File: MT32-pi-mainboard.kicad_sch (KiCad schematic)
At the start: 20 parts, among them J1 RPi, J2 MIDI In, J3 LCD2004, J4 5V, J5 LCD2004, SW1 Encoder, SW2 Button 1, SW3 Button 2, SW4 Power, U1 6N138

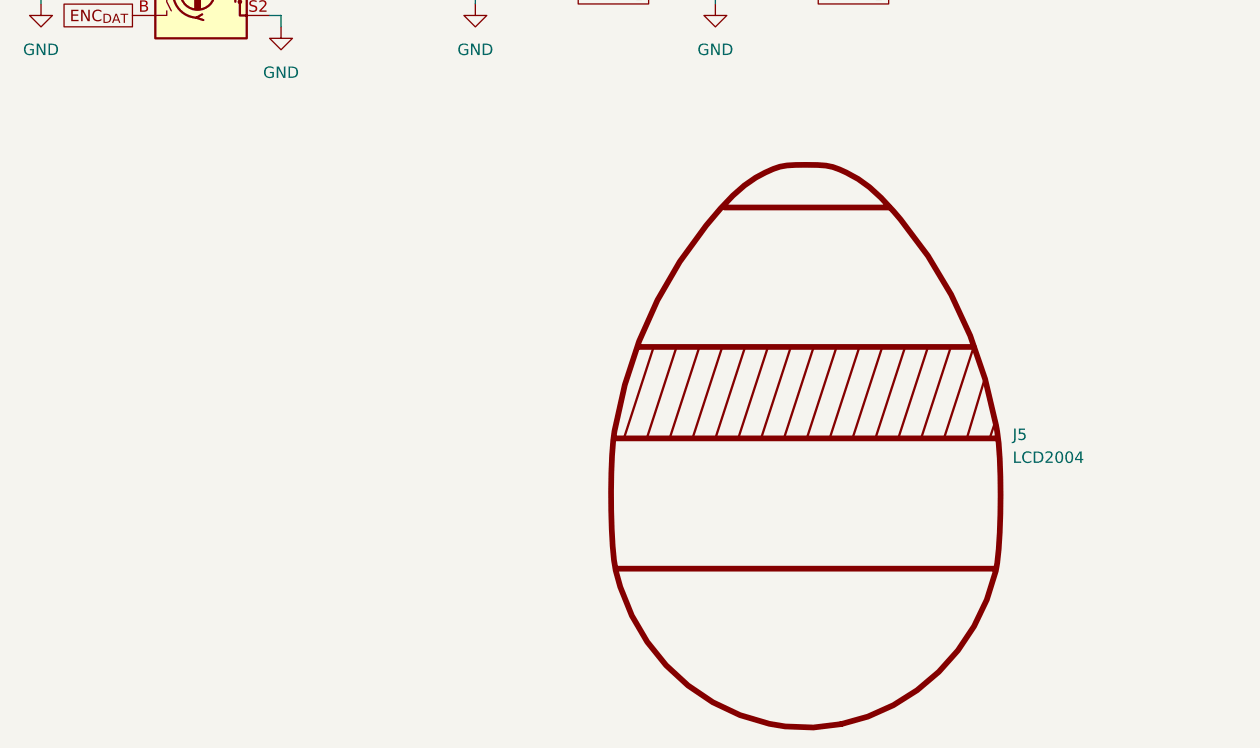
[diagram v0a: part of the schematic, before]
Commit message: add symbols for virtual models and graphics
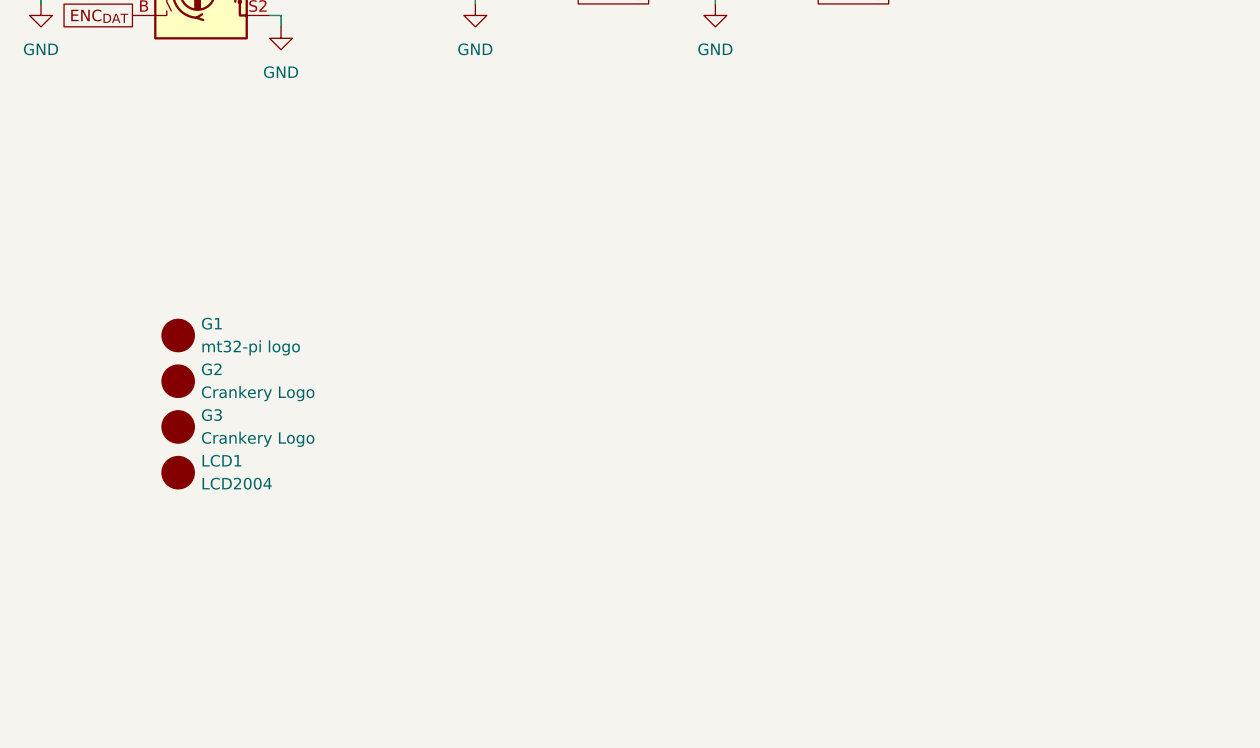
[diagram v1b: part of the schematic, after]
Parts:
- removed J5: LCD2004, 0:LCD2004, symbol Graphic:SYM_EasterEgg_42x60mm
- added G1: mt32-pi logo, 0:mt32-pi-logo, symbol 0:MT32-pi_Logo
- added G2, G3: Crankery Logo, 0:crankery_small, symbol 0:CrankeryLogo
- added LCD1: LCD2004, 0:LCD2004, symbol 0:LCD2004
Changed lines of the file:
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@@
-	)
-	(symbol
-		(lib_id "Graphic:SYM_EasterEgg_42x60mm")
-		(at 119.38 190.5 0)
-		(unit 1)
-		(exclude_from_sim no)
-		(in_bom no)
-		(on_board yes)
-		(dnp no)
-		(fields_autoplaced yes)
-		(property "Reference" "J5"
-			(at 142.24 158.3465 0)
-			(effects
-				(font
-					(size 1.27 1.27)
-				)
-				(justify left)
-			)
-		)
-		(property "Value" "LCD2004"
-			(at 142.24 160.8865 0)
-			(effects
-				(font
-					(size 1.27 1.27)
-				)
-				(justify left)
-			)
-		)
-		(property "Footprint" "0:LCD2004"
-			(at 119.38 194.31 0)
-			(effects
-				(font
-					(size 1.27 1.27)
-				)
-				(hide yes)
-			)
-		)
-		(property "Datasheet" "https://eur-lex.europa.eu/LexUriServ/LexUriServ.do?uri=OJ:L:2013:347:0671:0854:de:PDF"
-			(at 119.38 196.85 0)
-			(effects
-				(font
-					(size 1.27 1.27)
-				)
-				(hide yes)
-			)
-		)
-		(property "Description" "EasterEgg, ClassA, Medium Size"
-			(at 119.38 190.5 0)
-			(effects
-				(font
-					(size 1.27 1.27)
-				)
-				(hide yes)
-			)
-		)
-		(property "Sim.Enable" "0"
-			(at 119.38 193.04 0)
-			(effects
-				(font
-					(size 1.27 1.27)
-				)
-				(hide yes)
-			)
-		)
-		(instances
-			(project "MT32-pi-bo"
-				(path "/fe08e03c-4700-45c5-8be1-7bf60d684865"
-					(reference "J5")
-					(unit 1)
-				)
-			)
-		)
 	)
 	(symbol
@@
 	)
 	(symbol
+		(lib_id "0:CrankeryLogo")
+		(at 49.53 152.4 0)
+		(unit 1)
+		(exclude_from_sim no)
+		(in_bom no)
+		(on_board yes)
+		(dnp no)
+		(fields_autoplaced yes)
+		(property "Reference" "G2"
+			(at 52.07 151.1299 0)
+			(effects
+				(font
+					(size 1.27 1.27)
+				)
+				(justify left)
+			)
+		)
+		(property "Value" "Crankery Logo"
+			(at 52.07 153.6699 0)
+			(effects
+				(font
+					(size 1.27 1.27)
+				)
+				(justify left)
+			)
+		)
+		(property "Footprint" "0:crankery_small"
+			(at 49.53 152.4 0)
+			(effects
+				(font
+					(size 1.27 1.27)
+				)
+				(hide yes)
+			)
+		)
+		(property "Datasheet" ""
+			(at 49.53 152.4 0)
+			(effects
+				(font
+					(size 1.27 1.27)
+				)
+				(hide yes)
+			)
+		)
+		(property "Description" ""
+			(at 49.53 152.4 0)
+			(effects
+				(font
+					(size 1.27 1.27)
+				)
+				(hide yes)
+			)
+		)
+		(instances
+			(project ""
+				(path "/fe08e03c-4700-45c5-8be1-7bf60d684865"
+					(reference "G2")
+					(unit 1)
+				)
+			)
+		)
+	)
+	(symbol
 		(lib_id "0:GY-PCM5102")
 		(at 163.83 72.39 0)
@@
 				(path "/fe08e03c-4700-45c5-8be1-7bf60d684865"
 					(reference "U1")
+					(unit 1)
+				)
+			)
+		)
+	)
+	(symbol
+		(lib_id "0:LCD2004")
+		(at 49.53 162.56 0)
+		(unit 1)
+		(exclude_from_sim no)
+		(in_bom no)
+		(on_board yes)
+		(dnp no)
+		(fields_autoplaced yes)
+		(property "Reference" "LCD1"
+			(at 52.07 161.2899 0)
+			(effects
+				(font
+					(size 1.27 1.27)
+				)
+				(justify left)
+			)
+		)
+		(property "Value" "LCD2004"
+			(at 52.07 163.8299 0)
+			(effects
+				(font
+					(size 1.27 1.27)
+				)
+				(justify left)
+			)
+		)
+		(property "Footprint" "0:LCD2004"
+			(at 49.53 162.56 0)
+			(effects
+				(font
+					(size 1.27 1.27)
+				)
+				(hide yes)
+			)
+		)
+		(property "Datasheet" ""
+			(at 49.53 162.56 0)
+			(effects
+				(font
+					(size 1.27 1.27)
+				)
+				(hide yes)
+			)
+		)
+		(property "Description" ""
+			(at 49.53 162.56 0)
+			(effects
+				(font
+					(size 1.27 1.27)
+				)
+				(hide yes)
+			)
+		)
+		(instances
+			(project ""
+				(path "/fe08e03c-4700-45c5-8be1-7bf60d684865"
+					(reference "LCD1")
 					(unit 1)
 				)
@@
 	)
 	(symbol
+		(lib_id "0:CrankeryLogo")
+		(at 49.53 157.48 0)
+		(unit 1)
+		(exclude_from_sim no)
+		(in_bom no)
+		(on_board yes)
+		(dnp no)
+		(fields_autoplaced yes)
+		(property "Reference" "G3"
+			(at 52.07 156.2099 0)
+			(effects
+				(font
+					(size 1.27 1.27)
+				)
+				(justify left)
+			)
+		)
+		(property "Value" "Crankery Logo"
+			(at 52.07 158.7499 0)
+			(effects
+				(font
+					(size 1.27 1.27)
+				)
+				(justify left)
+			)
+		)
+		(property "Footprint" "0:crankery_small"
+			(at 49.53 157.48 0)
+			(effects
+				(font
+					(size 1.27 1.27)
+				)
+				(hide yes)
+			)
+		)
+		(property "Datasheet" ""
+			(at 49.53 157.48 0)
+			(effects
+				(font
+					(size 1.27 1.27)
+				)
+				(hide yes)
+			)
+		)
+		(property "Description" ""
+			(at 49.53 157.48 0)
+			(effects
+				(font
+					(size 1.27 1.27)
+				)
+				(hide yes)
+			)
+		)
+		(instances
+			(project "MT32-pi-mainboard"
+				(path "/fe08e03c-4700-45c5-8be1-7bf60d684865"
+					(reference "G3")
+					(unit 1)
+				)
+			)
+		)
+	)
+	(symbol
 		(lib_id "power:GND")
 		(at 156.21 33.02 0)
@@
 					(unit 1)
 				)
+			)
+		)
+	)
+	(symbol
+		(lib_id "0:MT32-pi_Logo")
+		(at 49.53 147.32 0)
+		(unit 1)
+		(exclude_from_sim no)
+		(in_bom no)
+		(on_board yes)
+		(dnp no)
+		(fields_autoplaced yes)
+		(property "Reference" "G1"
+			(at 52.07 146.0499 0)
+			(effects
+				(font
+					(size 1.27 1.27)
+				)
+				(justify left)
+			)
+		)
+		(property "Value" "mt32-pi logo"
+			(at 52.07 148.5899 0)
+			(effects
+				(font
+					(size 1.27 1.27)
+				)
+				(justify left)
+			)
+		)
+		(property "Footprint" "0:mt32-pi-logo"
+			(at 49.53 147.32 0)
+			(effects
+				(font
+					(size 1.27 1.27)
+				)
+				(hide yes)
+			)
+		)
+		(property "Datasheet" ""
+			(at 49.53 147.32 0)
+			(effects
+				(font
+					(size 1.27 1.27)
+				)
+				(hide yes)
+			)
+		)
+		(property "Description" ""
+			(at 49.53 147.32 0)
+			(effects
+				(font
+					(size 1.27 1.27)
+				)
+				(hide yes)
+			)
+		)
+		(instances
+			(project ""
+				(path "/fe08e03c-4700-45c5-8be1-7bf60d684865"
+					(reference "G1")
+					(unit 1)
+				)

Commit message: cleanup, add gerbers
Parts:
- D1: footprint Diode_THT:D_DO-35_SOD27_P7.62mm_Horizontal -> 0:D_DO-35_SOD27_P7.62mm_Horizontal
- J3: footprint Connector_PinSocket_2.54mm:PinSocket_1x16_P2.54mm_Horizontal -> 0:PinSocket_1x16_P2.54mm_Horizontal
- R1, R2, R3: footprint Resistor_THT:R_Axial_DIN0207_L6.3mm_D2.5mm_P7.62mm_Horizontal -> 0:R_Axial_DIN0207_L6.3mm_D2.5mm_P7.62mm_Horizontal
- U1: footprint Package_DIP:DIP-8_W7.62mm -> 0:DIP-8_W7.62mm
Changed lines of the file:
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@@
 			)
 		)
-		(property "Footprint" "Connector_PinSocket_2.54mm:PinSocket_1x16_P2.54mm_Horizontal"
+		(property "Footprint" "0:PinSocket_1x16_P2.54mm_Horizontal"
 			(at 228.6 130.81 0)
 			(effects
@@
 			)
 		)
-		(property "Footprint" "Package_DIP:DIP-8_W7.62mm"
+		(property "Footprint" "0:DIP-8_W7.62mm"
 			(at 216.916 43.18 0)
 			(effects
@@
 	(symbol
 		(lib_id "Mechanical:MountingHole")
-		(at 213.36 73.66 0)
+		(at 49.53 172.72 0)
 		(unit 1)
 		(exclude_from_sim no)
@@
 		(fields_autoplaced yes)
 		(property "Reference" "H3"
-			(at 215.9 72.3899 0)
+			(at 52.07 171.4499 0)
 			(effects
 				(font
@@
 		)
 		(property "Value" "MountingHole"
-			(at 215.9 73.6599 0)
+			(at 52.07 172.7199 0)
 			(effects
 				(font
@@
 		)
 		(property "Footprint" "0:MountingHole_2.7mm_M2.5"
-			(at 213.36 73.66 0)
+			(at 49.53 172.72 0)
 			(effects
 				(font
@@
 		)
 		(property "Datasheet" "~"
-			(at 213.36 73.66 0)
+			(at 49.53 172.72 0)
 			(effects
 				(font
@@
 		)
 		(property "Description" "Mounting Hole without connection"
-			(at 213.36 73.66 0)
+			(at 49.53 172.72 0)
 			(effects
 				(font
@@
 			)
 		)
-		(property "Footprint" "Resistor_THT:R_Axial_DIN0207_L6.3mm_D2.5mm_P7.62mm_Horizontal"
+		(property "Footprint" "0:R_Axial_DIN0207_L6.3mm_D2.5mm_P7.62mm_Horizontal"
 			(at 226.06 32.258 90)
 			(effects
@@
 			)
 		)
-		(property "Footprint" "Diode_THT:D_DO-35_SOD27_P7.62mm_Horizontal"
+		(property "Footprint" "0:D_DO-35_SOD27_P7.62mm_Horizontal"
 			(at 194.31 41.91 0)
 			(effects
@@
 			)
 		)
-		(property "Footprint" "Resistor_THT:R_Axial_DIN0207_L6.3mm_D2.5mm_P7.62mm_Horizontal"
+		(property "Footprint" "0:R_Axial_DIN0207_L6.3mm_D2.5mm_P7.62mm_Horizontal"
 			(at 204.47 150.368 90)
 			(effects
@@
 	(symbol
 		(lib_id "Mechanical:MountingHole")
-		(at 209.55 73.66 0)
+		(at 49.53 167.64 0)
 		(unit 1)
 		(exclude_from_sim no)
@@
 		(fields_autoplaced yes)
 		(property "Reference" "H2"
-			(at 212.09 72.3899 0)
+			(at 52.07 166.3699 0)
 			(effects
 				(font
@@
 		)
 		(property "Value" "MountingHole"
-			(at 212.09 73.6599 0)
+			(at 52.07 167.6399 0)
 			(effects
 				(font
@@
 		)
 		(property "Footprint" "0:MountingHole_2.7mm_M2.5"
-			(at 209.55 73.66 0)
+			(at 49.53 167.64 0)
 			(effects
 				(font
@@
 		)
 		(property "Datasheet" "~"
-			(at 209.55 73.66 0)
+			(at 49.53 167.64 0)
 			(effects
 				(font
@@
 		)
 		(property "Description" "Mounting Hole without connection"
-			(at 209.55 73.66 0)
+			(at 49.53 167.64 0)
 			(effects
 				(font
@@
 			)
 		)
-		(property "Footprint" "Resistor_THT:R_Axial_DIN0207_L6.3mm_D2.5mm_P7.62mm_Horizontal"
+		(property "Footprint" "0:R_Axial_DIN0207_L6.3mm_D2.5mm_P7.62mm_Horizontal"
 			(at 189.23 34.798 90)
 			(effects

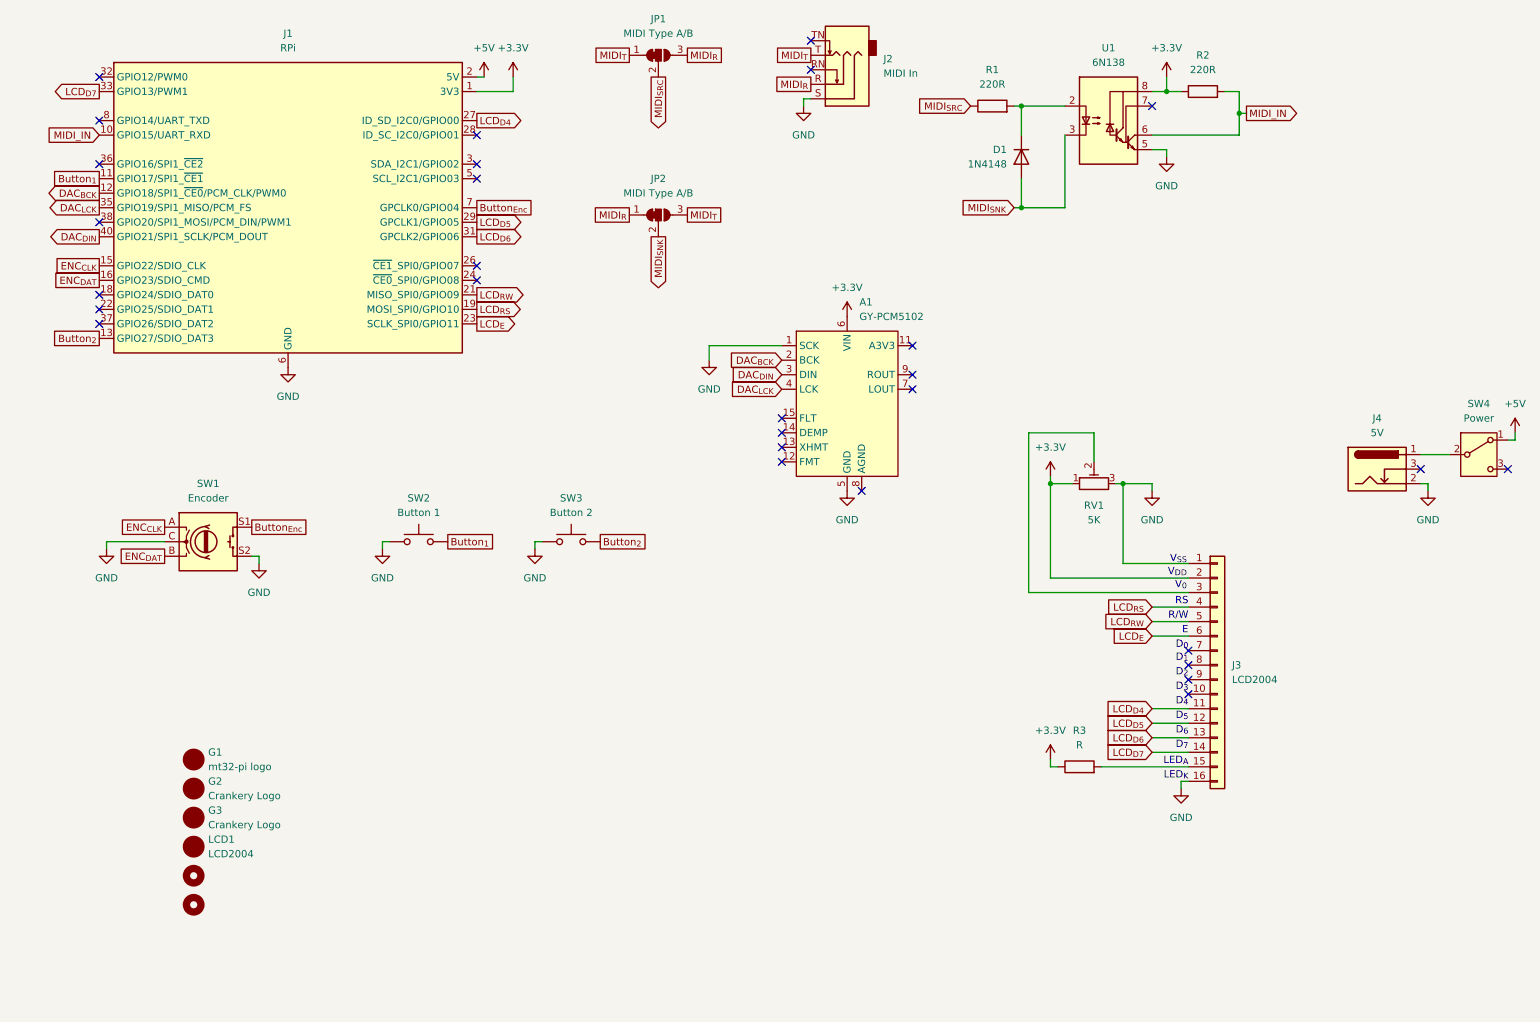
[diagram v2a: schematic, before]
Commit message: clean up silks, use project properties for text
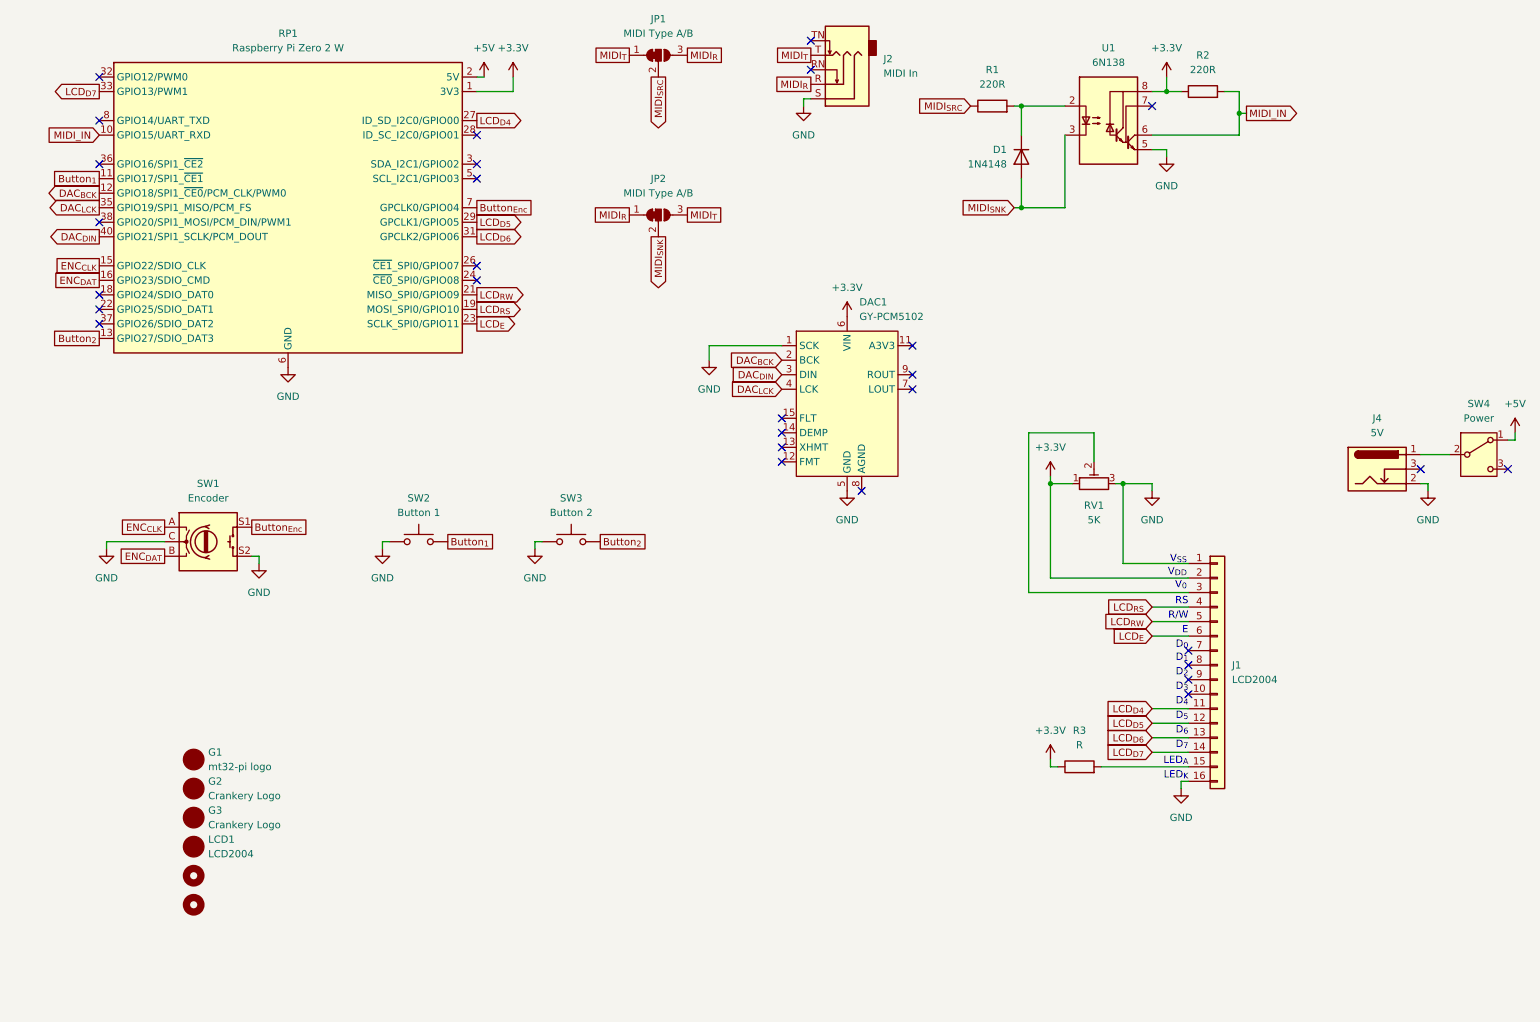
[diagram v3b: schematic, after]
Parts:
- RP1: renamed from J1; value RPi -> Raspberry Pi Zero 2 W
- renumbered A1 to DAC1, J3 to J1
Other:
- company: (none) -> ${Company}
- title: (none) -> ${Title}
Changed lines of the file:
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@@
 	(generator "eeschema")
 	(generator_version "9.0")
-	(paper "A4")
+	(paper "USLetter")
+	(title_block
+		(title "${Title}")
+		(date "${Issue_Date}")
+		(rev "${Revision}")
+		(company "${Company}")
+		(comment 1 "${Author}")
+		(comment 2 "${Github}")
+	)
 	(text "D_{7}"
 		(exclude_from_sim no)
@@
 		(dnp no)
 		(fields_autoplaced yes)
-		(property "Reference" "A1"
+		(property "Reference" "DAC1"
 			(at 165.9733 67.31 0)
 			(effects
@@
 			(project ""
 				(path "/fe08e03c-4700-45c5-8be1-7bf60d684865"
-					(reference "A1")
+					(reference "DAC1")
 					(unit 1)
 				)
@@
 		(dnp no)
 		(fields_autoplaced yes)
-		(property "Reference" "J3"
+		(property "Reference" "J1"
 			(at 231.14 130.8099 0)
 			(effects
@@
 			(project ""
 				(path "/fe08e03c-4700-45c5-8be1-7bf60d684865"
-					(reference "J3")
+					(reference "J1")
 					(unit 1)
 				)
@@
 		(dnp no)
 		(fields_autoplaced yes)
-		(property "Reference" "J1"
+		(property "Reference" "RP1"
 			(at 66.04 20.32 0)
 			(effects
@@
 			)
 		)
-		(property "Value" "RPi"
+		(property "Value" "Raspberry Pi Zero 2 W"
 			(at 66.04 22.86 0)
 			(effects
@@
 			(project ""
 				(path "/fe08e03c-4700-45c5-8be1-7bf60d684865"
-					(reference "J1")
+					(reference "RP1")
 					(unit 1)
 				)
